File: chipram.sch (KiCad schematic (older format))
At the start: 28 parts, among them J500 Jumper_2_Bridged, U500 62402, U501 XX4256-15, U502 XX4256-15, U503 XX4256-15, U504 XX4256-15, U505 XX4256-15, U506 XX4256-15, U507 XX4256-15, U508 XX4256-15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

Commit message: Update footprints
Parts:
- C500, C501, C502, C503, C504, C505, C506, C507, C508, C540, C541: footprint (none) -> Capacitor_THT:C_Rect_L11.0mm_W2.8mm_P10.00mm_MKT
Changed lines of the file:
@@
 F 0 "C500" V 2848 10700 50  0000 C CNN
 F 1 "0.22uF" V 2939 10700 50  0000 C CNN
-F 2 "" H 3138 10550 50  0001 C CNN
+F 2 "Capacitor_THT:C_Rect_L11.0mm_W2.8mm_P10.00mm_MKT" H 3138 10550 50  0001 C CNN
 F 3 "~" H 3100 10700 50  0001 C CNN
 	1    3100 10700
@@
 F 0 "C501" V 7548 4300 50  0000 C CNN
 F 1 "0.33uF" V 7639 4300 50  0000 C CNN
-F 2 "" H 7838 4150 50  0001 C CNN
+F 2 "Capacitor_THT:C_Rect_L11.0mm_W2.8mm_P10.00mm_MKT" H 7838 4150 50  0001 C CNN
 F 3 "~" H 7800 4300 50  0001 C CNN
 	1    7800 4300
@@
 F 0 "C502" V 10048 4300 50  0000 C CNN
 F 1 "0.33uF" V 10139 4300 50  0000 C CNN
-F 2 "" H 10338 4150 50  0001 C CNN
+F 2 "Capacitor_THT:C_Rect_L11.0mm_W2.8mm_P10.00mm_MKT" H 10338 4150 50  0001 C CNN
 F 3 "~" H 10300 4300 50  0001 C CNN
 	1    10300 4300
@@
 F 0 "C503" V 12548 4300 50  0000 C CNN
 F 1 "0.33uF" V 12639 4300 50  0000 C CNN
-F 2 "" H 12838 4150 50  0001 C CNN
+F 2 "Capacitor_THT:C_Rect_L11.0mm_W2.8mm_P10.00mm_MKT" H 12838 4150 50  0001 C CNN
 F 3 "~" H 12800 4300 50  0001 C CNN
 	1    12800 4300
@@
 F 0 "C504" V 14548 4300 50  0000 C CNN
 F 1 "0.33uF" V 14639 4300 50  0000 C CNN
-F 2 "" H 14838 4150 50  0001 C CNN
+F 2 "Capacitor_THT:C_Rect_L11.0mm_W2.8mm_P10.00mm_MKT" H 14838 4150 50  0001 C CNN
 F 3 "~" H 14800 4300 50  0001 C CNN
 	1    14800 4300
@@
 F 0 "C508" V 14548 7300 50  0000 C CNN
 F 1 "0.33uF" V 14639 7300 50  0000 C CNN
-F 2 "" H 14838 7150 50  0001 C CNN
+F 2 "Capacitor_THT:C_Rect_L11.0mm_W2.8mm_P10.00mm_MKT" H 14838 7150 50  0001 C CNN
 F 3 "~" H 14800 7300 50  0001 C CNN
 	1    14800 7300
@@
 F 0 "C507" V 12498 7300 50  0000 C CNN
 F 1 "0.33uF" V 12589 7300 50  0000 C CNN
-F 2 "" H 12788 7150 50  0001 C CNN
+F 2 "Capacitor_THT:C_Rect_L11.0mm_W2.8mm_P10.00mm_MKT" H 12788 7150 50  0001 C CNN
 F 3 "~" H 12750 7300 50  0001 C CNN
 	1    12750 7300
@@
 F 0 "C506" V 10048 7300 50  0000 C CNN
 F 1 "0.33uF" V 10139 7300 50  0000 C CNN
-F 2 "" H 10338 7150 50  0001 C CNN
+F 2 "Capacitor_THT:C_Rect_L11.0mm_W2.8mm_P10.00mm_MKT" H 10338 7150 50  0001 C CNN
 F 3 "~" H 10300 7300 50  0001 C CNN
 	1    10300 7300
@@
 F 0 "C505" V 7548 7300 50  0000 C CNN
 F 1 "0.33uF" V 7639 7300 50  0000 C CNN
-F 2 "" H 7838 7150 50  0001 C CNN
+F 2 "Capacitor_THT:C_Rect_L11.0mm_W2.8mm_P10.00mm_MKT" H 7838 7150 50  0001 C CNN
 F 3 "~" H 7800 7300 50  0001 C CNN
 	1    7800 7300
@@
 F 0 "C540" H 2565 896 50  0000 L CNN
 F 1 "0.1uF" H 2565 805 50  0000 L CNN
-F 2 "" H 2488 700 50  0001 C CNN
+F 2 "Capacitor_THT:C_Rect_L11.0mm_W2.8mm_P10.00mm_MKT" H 2488 700 50  0001 C CNN
 F 3 "~" H 2450 850 50  0001 C CNN
 	1    2450 850
@@
 F 0 "C541" H 2615 2846 50  0000 L CNN
 F 1 "0.1uF" H 2615 2755 50  0000 L CNN
-F 2 "" H 2538 2650 50  0001 C CNN
+F 2 "Capacitor_THT:C_Rect_L11.0mm_W2.8mm_P10.00mm_MKT" H 2538 2650 50  0001 C CNN
 F 3 "~" H 2500 2800 50  0001 C CNN
 	1    2500 2800

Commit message: More placement
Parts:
- J500: footprint Connector_PinSocket_2.54mm:PinSocket_2x01_P2.54mm_Vertical -> Connector_PinHeader_2.54mm:PinHeader_2x01_P2.54mm_Vertical
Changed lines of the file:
@@
 F 0 "J500" H 1750 7603 50  0000 C CNN
 F 1 "Jumper_2_Bridged" H 1750 7604 50  0001 C CNN
-F 2 "Connector_PinSocket_2.54mm:PinSocket_2x01_P2.54mm_Vertical" H 1750 7500 50  0001 C CNN
+F 2 "Connector_PinHeader_2.54mm:PinHeader_2x01_P2.54mm_Vertical" H 1750 7500 50  0001 C CNN
 F 3 "~" H 1750 7500 50  0001 C CNN
 	1    1750 7500

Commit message: Make caps footprint smaller
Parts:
- C500, C501, C502, C503, C504, C505, C506, C507, C508, C540, C541: footprint Capacitor_THT:C_Rect_L11.0mm_W2.8mm_P10.00mm_MKT -> Capacitor_THT:C_Rect_L11.5mm_W2.0mm_P10.00mm_MKT
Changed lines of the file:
@@
 F 0 "C500" V 2848 10700 50  0000 C CNN
 F 1 "0.22uF" V 2939 10700 50  0000 C CNN
-F 2 "Capacitor_THT:C_Rect_L11.0mm_W2.8mm_P10.00mm_MKT" H 3138 10550 50  0001 C CNN
+F 2 "Capacitor_THT:C_Rect_L11.5mm_W2.0mm_P10.00mm_MKT" H 3138 10550 50  0001 C CNN
 F 3 "~" H 3100 10700 50  0001 C CNN
 	1    3100 10700
@@
 F 0 "C501" V 7548 4300 50  0000 C CNN
 F 1 "0.33uF" V 7639 4300 50  0000 C CNN
-F 2 "Capacitor_THT:C_Rect_L11.0mm_W2.8mm_P10.00mm_MKT" H 7838 4150 50  0001 C CNN
+F 2 "Capacitor_THT:C_Rect_L11.5mm_W2.0mm_P10.00mm_MKT" H 7838 4150 50  0001 C CNN
 F 3 "~" H 7800 4300 50  0001 C CNN
 	1    7800 4300
@@
 F 0 "C502" V 10048 4300 50  0000 C CNN
 F 1 "0.33uF" V 10139 4300 50  0000 C CNN
-F 2 "Capacitor_THT:C_Rect_L11.0mm_W2.8mm_P10.00mm_MKT" H 10338 4150 50  0001 C CNN
+F 2 "Capacitor_THT:C_Rect_L11.5mm_W2.0mm_P10.00mm_MKT" H 10338 4150 50  0001 C CNN
 F 3 "~" H 10300 4300 50  0001 C CNN
 	1    10300 4300
@@
 F 0 "C503" V 12548 4300 50  0000 C CNN
 F 1 "0.33uF" V 12639 4300 50  0000 C CNN
-F 2 "Capacitor_THT:C_Rect_L11.0mm_W2.8mm_P10.00mm_MKT" H 12838 4150 50  0001 C CNN
+F 2 "Capacitor_THT:C_Rect_L11.5mm_W2.0mm_P10.00mm_MKT" H 12838 4150 50  0001 C CNN
 F 3 "~" H 12800 4300 50  0001 C CNN
 	1    12800 4300
@@
 F 0 "C504" V 14548 4300 50  0000 C CNN
 F 1 "0.33uF" V 14639 4300 50  0000 C CNN
-F 2 "Capacitor_THT:C_Rect_L11.0mm_W2.8mm_P10.00mm_MKT" H 14838 4150 50  0001 C CNN
+F 2 "Capacitor_THT:C_Rect_L11.5mm_W2.0mm_P10.00mm_MKT" H 14838 4150 50  0001 C CNN
 F 3 "~" H 14800 4300 50  0001 C CNN
 	1    14800 4300
@@
 F 0 "C508" V 14548 7300 50  0000 C CNN
 F 1 "0.33uF" V 14639 7300 50  0000 C CNN
-F 2 "Capacitor_THT:C_Rect_L11.0mm_W2.8mm_P10.00mm_MKT" H 14838 7150 50  0001 C CNN
+F 2 "Capacitor_THT:C_Rect_L11.5mm_W2.0mm_P10.00mm_MKT" H 14838 7150 50  0001 C CNN
 F 3 "~" H 14800 7300 50  0001 C CNN
 	1    14800 7300
@@
 F 0 "C507" V 12498 7300 50  0000 C CNN
 F 1 "0.33uF" V 12589 7300 50  0000 C CNN
-F 2 "Capacitor_THT:C_Rect_L11.0mm_W2.8mm_P10.00mm_MKT" H 12788 7150 50  0001 C CNN
+F 2 "Capacitor_THT:C_Rect_L11.5mm_W2.0mm_P10.00mm_MKT" H 12788 7150 50  0001 C CNN
 F 3 "~" H 12750 7300 50  0001 C CNN
 	1    12750 7300
@@
 F 0 "C506" V 10048 7300 50  0000 C CNN
 F 1 "0.33uF" V 10139 7300 50  0000 C CNN
-F 2 "Capacitor_THT:C_Rect_L11.0mm_W2.8mm_P10.00mm_MKT" H 10338 7150 50  0001 C CNN
+F 2 "Capacitor_THT:C_Rect_L11.5mm_W2.0mm_P10.00mm_MKT" H 10338 7150 50  0001 C CNN
 F 3 "~" H 10300 7300 50  0001 C CNN
 	1    10300 7300
@@
 F 0 "C505" V 7548 7300 50  0000 C CNN
 F 1 "0.33uF" V 7639 7300 50  0000 C CNN
-F 2 "Capacitor_THT:C_Rect_L11.0mm_W2.8mm_P10.00mm_MKT" H 7838 7150 50  0001 C CNN
+F 2 "Capacitor_THT:C_Rect_L11.5mm_W2.0mm_P10.00mm_MKT" H 7838 7150 50  0001 C CNN
 F 3 "~" H 7800 7300 50  0001 C CNN
 	1    7800 7300
@@
 F 0 "C540" H 2565 896 50  0000 L CNN
 F 1 "0.1uF" H 2565 805 50  0000 L CNN
-F 2 "Capacitor_THT:C_Rect_L11.0mm_W2.8mm_P10.00mm_MKT" H 2488 700 50  0001 C CNN
+F 2 "Capacitor_THT:C_Rect_L11.5mm_W2.0mm_P10.00mm_MKT" H 2488 700 50  0001 C CNN
 F 3 "~" H 2450 850 50  0001 C CNN
 	1    2450 850
@@
 F 0 "C541" H 2615 2846 50  0000 L CNN
 F 1 "0.1uF" H 2615 2755 50  0000 L CNN
-F 2 "Capacitor_THT:C_Rect_L11.0mm_W2.8mm_P10.00mm_MKT" H 2538 2650 50  0001 C CNN
+F 2 "Capacitor_THT:C_Rect_L11.5mm_W2.0mm_P10.00mm_MKT" H 2538 2650 50  0001 C CNN
 F 3 "~" H 2500 2800 50  0001 C CNN
 	1    2500 2800

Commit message: Switch footprints for suitable modern replacements
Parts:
- C500, C501, C502, C503, C504, C505, C506, C507, C508: footprint Capacitor_THT:C_Rect_L11.5mm_W2.0mm_P10.00mm_MKT -> Capacitor_THT:C_Rect_L11.5mm_W4.0mm_P10.00mm_MKT
- C540, C541: footprint Capacitor_THT:C_Rect_L11.5mm_W2.0mm_P10.00mm_MKT -> Capacitor_THT:C_Rect_L11.5mm_W2.6mm_P10.00mm_MKT
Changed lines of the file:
@@
 F 0 "C500" V 2848 10700 50  0000 C CNN
 F 1 "0.22uF" V 2939 10700 50  0000 C CNN
-F 2 "Capacitor_THT:C_Rect_L11.5mm_W2.0mm_P10.00mm_MKT" H 3138 10550 50  0001 C CNN
+F 2 "Capacitor_THT:C_Rect_L11.5mm_W4.0mm_P10.00mm_MKT" H 3138 10550 50  0001 C CNN
 F 3 "~" H 3100 10700 50  0001 C CNN
 	1    3100 10700
@@
 F 0 "C501" V 7548 4300 50  0000 C CNN
 F 1 "0.33uF" V 7639 4300 50  0000 C CNN
-F 2 "Capacitor_THT:C_Rect_L11.5mm_W2.0mm_P10.00mm_MKT" H 7838 4150 50  0001 C CNN
+F 2 "Capacitor_THT:C_Rect_L11.5mm_W4.0mm_P10.00mm_MKT" H 7838 4150 50  0001 C CNN
 F 3 "~" H 7800 4300 50  0001 C CNN
 	1    7800 4300
@@
 F 0 "C502" V 10048 4300 50  0000 C CNN
 F 1 "0.33uF" V 10139 4300 50  0000 C CNN
-F 2 "Capacitor_THT:C_Rect_L11.5mm_W2.0mm_P10.00mm_MKT" H 10338 4150 50  0001 C CNN
+F 2 "Capacitor_THT:C_Rect_L11.5mm_W4.0mm_P10.00mm_MKT" H 10338 4150 50  0001 C CNN
 F 3 "~" H 10300 4300 50  0001 C CNN
 	1    10300 4300
@@
 F 0 "C503" V 12548 4300 50  0000 C CNN
 F 1 "0.33uF" V 12639 4300 50  0000 C CNN
-F 2 "Capacitor_THT:C_Rect_L11.5mm_W2.0mm_P10.00mm_MKT" H 12838 4150 50  0001 C CNN
+F 2 "Capacitor_THT:C_Rect_L11.5mm_W4.0mm_P10.00mm_MKT" H 12838 4150 50  0001 C CNN
 F 3 "~" H 12800 4300 50  0001 C CNN
 	1    12800 4300
@@
 F 0 "C504" V 14548 4300 50  0000 C CNN
 F 1 "0.33uF" V 14639 4300 50  0000 C CNN
-F 2 "Capacitor_THT:C_Rect_L11.5mm_W2.0mm_P10.00mm_MKT" H 14838 4150 50  0001 C CNN
+F 2 "Capacitor_THT:C_Rect_L11.5mm_W4.0mm_P10.00mm_MKT" H 14838 4150 50  0001 C CNN
 F 3 "~" H 14800 4300 50  0001 C CNN
 	1    14800 4300
@@
 F 0 "C508" V 14548 7300 50  0000 C CNN
 F 1 "0.33uF" V 14639 7300 50  0000 C CNN
-F 2 "Capacitor_THT:C_Rect_L11.5mm_W2.0mm_P10.00mm_MKT" H 14838 7150 50  0001 C CNN
+F 2 "Capacitor_THT:C_Rect_L11.5mm_W4.0mm_P10.00mm_MKT" H 14838 7150 50  0001 C CNN
 F 3 "~" H 14800 7300 50  0001 C CNN
 	1    14800 7300
@@
 F 0 "C507" V 12498 7300 50  0000 C CNN
 F 1 "0.33uF" V 12589 7300 50  0000 C CNN
-F 2 "Capacitor_THT:C_Rect_L11.5mm_W2.0mm_P10.00mm_MKT" H 12788 7150 50  0001 C CNN
+F 2 "Capacitor_THT:C_Rect_L11.5mm_W4.0mm_P10.00mm_MKT" H 12788 7150 50  0001 C CNN
 F 3 "~" H 12750 7300 50  0001 C CNN
 	1    12750 7300
@@
 F 0 "C506" V 10048 7300 50  0000 C CNN
 F 1 "0.33uF" V 10139 7300 50  0000 C CNN
-F 2 "Capacitor_THT:C_Rect_L11.5mm_W2.0mm_P10.00mm_MKT" H 10338 7150 50  0001 C CNN
+F 2 "Capacitor_THT:C_Rect_L11.5mm_W4.0mm_P10.00mm_MKT" H 10338 7150 50  0001 C CNN
 F 3 "~" H 10300 7300 50  0001 C CNN
 	1    10300 7300
@@
 F 0 "C505" V 7548 7300 50  0000 C CNN
 F 1 "0.33uF" V 7639 7300 50  0000 C CNN
-F 2 "Capacitor_THT:C_Rect_L11.5mm_W2.0mm_P10.00mm_MKT" H 7838 7150 50  0001 C CNN
+F 2 "Capacitor_THT:C_Rect_L11.5mm_W4.0mm_P10.00mm_MKT" H 7838 7150 50  0001 C CNN
 F 3 "~" H 7800 7300 50  0001 C CNN
 	1    7800 7300
@@
 F 0 "C540" H 2565 896 50  0000 L CNN
 F 1 "0.1uF" H 2565 805 50  0000 L CNN
-F 2 "Capacitor_THT:C_Rect_L11.5mm_W2.0mm_P10.00mm_MKT" H 2488 700 50  0001 C CNN
+F 2 "Capacitor_THT:C_Rect_L11.5mm_W2.6mm_P10.00mm_MKT" H 2488 700 50  0001 C CNN
 F 3 "~" H 2450 850 50  0001 C CNN
 	1    2450 850
@@
 F 0 "C541" H 2615 2846 50  0000 L CNN
 F 1 "0.1uF" H 2615 2755 50  0000 L CNN
-F 2 "Capacitor_THT:C_Rect_L11.5mm_W2.0mm_P10.00mm_MKT" H 2538 2650 50  0001 C CNN
+F 2 "Capacitor_THT:C_Rect_L11.5mm_W2.6mm_P10.00mm_MKT" H 2538 2650 50  0001 C CNN
 F 3 "~" H 2500 2800 50  0001 C CNN
 	1    2500 2800

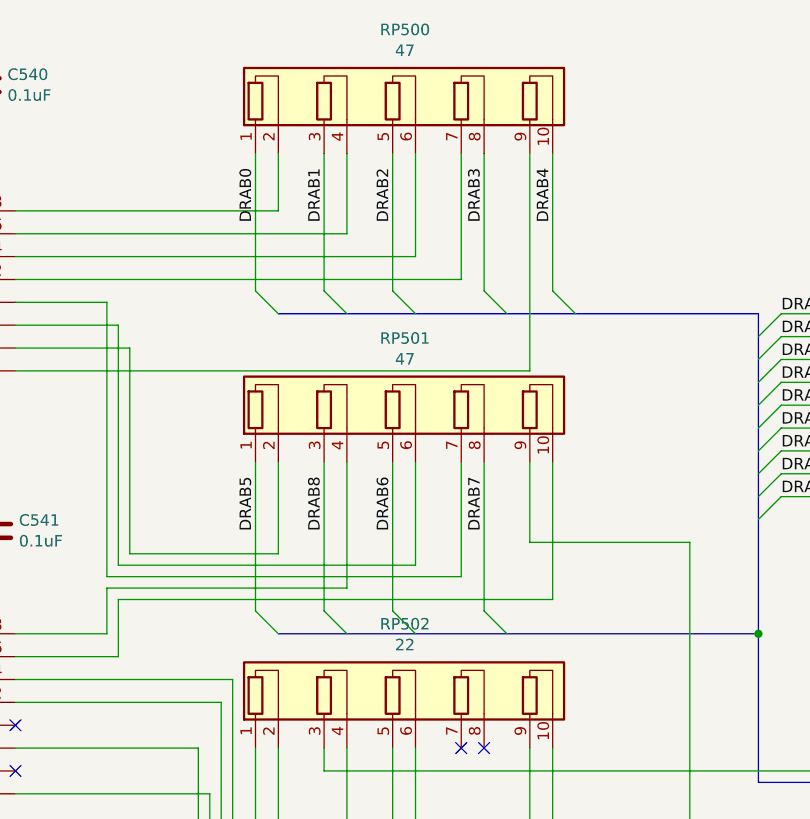
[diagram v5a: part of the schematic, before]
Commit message: Some footprints updates; Add all Mouser references
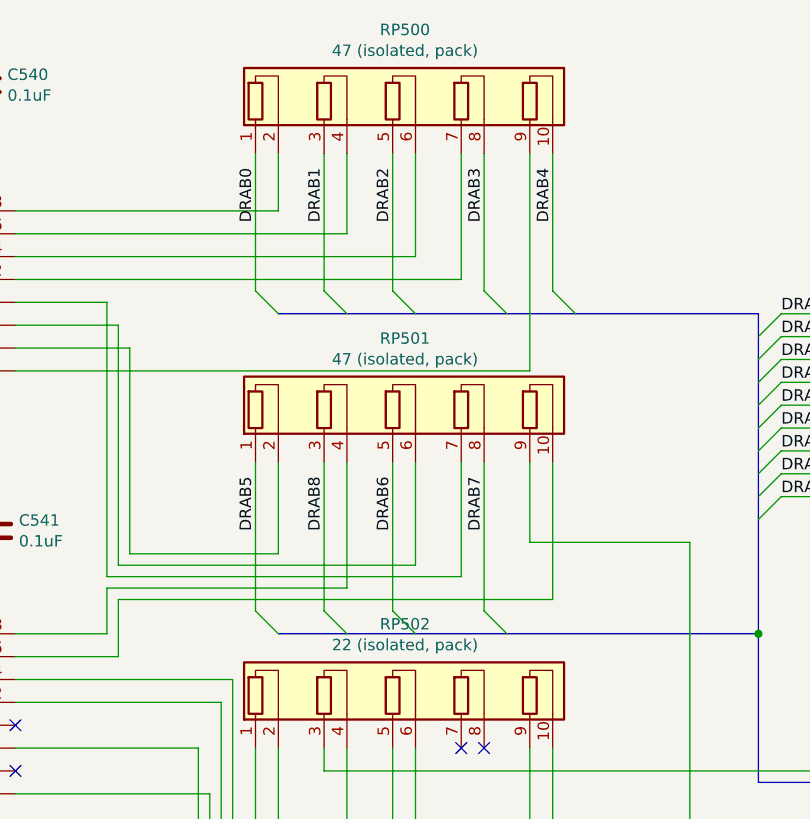
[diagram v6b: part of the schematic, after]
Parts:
- C500: RefOrder (none) -> 594-A224K20X7RF5TAA
- C501, C502, C503, C504, C505, C506, C507, C508: RefOrder (none) -> 581-SA305C334KAA
- C540, C541: RefOrder (none) -> 581-SA105C104KARC
- R500: RefOrder (none) -> 603-CFR-25JT-52-4K7
- RP500, RP501: value 47 -> 47 (isolated, pack); RefOrder (none) -> 652-4610X-2LF-47
- RP502: value 22 -> 22 (isolated, pack); RefOrder (none) -> 652-4610X-2LF-22
- RP503: RefOrder (none) -> 652-4610X-1LF-470
- U540, U541: RefOrder (none) -> 595-SN74F244N
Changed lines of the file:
@@
 F 2 "Package_DIP:DIP-20_W7.62mm_Socket" H 2100 1900 50  0001 C CNN
 F 3 "http://www.ti.com/lit/gpn/sn74F244" H 2100 1900 50  0001 C CNN
+F 4 "595-SN74F244N" H 2100 1900 50  0001 C CNN "RefOrder"
 	1    2100 1900
 	1    0    0    -1
@@
 F 2 "Package_DIP:DIP-20_W7.62mm_Socket" H 2100 3750 50  0001 C CNN
 F 3 "http://www.ti.com/lit/gpn/sn74F244" H 2100 3750 50  0001 C CNN
+F 4 "595-SN74F244N" H 2100 3750 50  0001 C CNN "RefOrder"
 	1    2100 3750
 	1    0    0    -1
@@
 F 2 "Capacitor_THT:C_Rect_L11.5mm_W4.0mm_P10.00mm_MKT" H 3138 10550 50  0001 C CNN
 F 3 "~" H 3100 10700 50  0001 C CNN
+F 4 "594-A224K20X7RF5TAA" H 3100 10700 50  0001 C CNN "RefOrder"
 	1    3100 10700
 	0    1    1    0
@@
 F 2 "Resistor_THT:R_Axial_DIN0207_L6.3mm_D2.5mm_P10.16mm_Horizontal" V 1230 7250 50  0001 C CNN
 F 3 "~" H 1300 7250 50  0001 C CNN
+F 4 "603-CFR-25JT-52-4K7" H 1300 7250 50  0001 C CNN "RefOrder"
 	1    1300 7250
 	1    0    0    -1
@@
 F 2 "Capacitor_THT:C_Rect_L11.5mm_W4.0mm_P10.00mm_MKT" H 7838 4150 50  0001 C CNN
 F 3 "~" H 7800 4300 50  0001 C CNN
+F 4 "581-SA305C334KAA" H 7800 4300 50  0001 C CNN "RefOrder"
 	1    7800 4300
 	0    1    1    0
@@
 F 2 "Capacitor_THT:C_Rect_L11.5mm_W4.0mm_P10.00mm_MKT" H 10338 4150 50  0001 C CNN
 F 3 "~" H 10300 4300 50  0001 C CNN
+F 4 "581-SA305C334KAA" H 10300 4300 50  0001 C CNN "RefOrder"
 	1    10300 4300
 	0    1    1    0
@@
 F 2 "Capacitor_THT:C_Rect_L11.5mm_W4.0mm_P10.00mm_MKT" H 12838 4150 50  0001 C CNN
 F 3 "~" H 12800 4300 50  0001 C CNN
+F 4 "581-SA305C334KAA" H 12800 4300 50  0001 C CNN "RefOrder"
 	1    12800 4300
 	0    1    1    0
@@
 F 2 "Capacitor_THT:C_Rect_L11.5mm_W4.0mm_P10.00mm_MKT" H 14838 4150 50  0001 C CNN
 F 3 "~" H 14800 4300 50  0001 C CNN
+F 4 "581-SA305C334KAA" H 14800 4300 50  0001 C CNN "RefOrder"
 	1    14800 4300
 	0    1    1    0
@@
 F 2 "Capacitor_THT:C_Rect_L11.5mm_W4.0mm_P10.00mm_MKT" H 14838 7150 50  0001 C CNN
 F 3 "~" H 14800 7300 50  0001 C CNN
+F 4 "581-SA305C334KAA" H 14800 7300 50  0001 C CNN "RefOrder"
 	1    14800 7300
 	0    1    1    0
@@
 F 2 "Capacitor_THT:C_Rect_L11.5mm_W4.0mm_P10.00mm_MKT" H 12788 7150 50  0001 C CNN
 F 3 "~" H 12750 7300 50  0001 C CNN
+F 4 "581-SA305C334KAA" H 12750 7300 50  0001 C CNN "RefOrder"
 	1    12750 7300
 	0    1    1    0
@@
 F 2 "Capacitor_THT:C_Rect_L11.5mm_W4.0mm_P10.00mm_MKT" H 10338 7150 50  0001 C CNN
 F 3 "~" H 10300 7300 50  0001 C CNN
+F 4 "581-SA305C334KAA" H 10300 7300 50  0001 C CNN "RefOrder"
 	1    10300 7300
 	0    1    1    0
@@
 F 2 "Capacitor_THT:C_Rect_L11.5mm_W4.0mm_P10.00mm_MKT" H 7838 7150 50  0001 C CNN
 F 3 "~" H 7800 7300 50  0001 C CNN
+F 4 "581-SA305C334KAA" H 7800 7300 50  0001 C CNN "RefOrder"
 	1    7800 7300
 	0    1    1    0
@@
 F 2 "Resistor_THT:R_Array_SIP10" V 7125 2250 50  0001 C CNN
 F 3 "http://www.vishay.com/docs/31509/csc.pdf" H 6550 2250 50  0001 C CNN
+F 4 "652-4610X-1LF-470" H 6550 2250 50  0001 C CNN "RefOrder"
 	1    6550 2250
 	0    1    1    0
@@
 P 4250 950
 F 0 "RP500" H 4304 1292 50  0000 C CNN
-F 1 "47" H 4304 1201 50  0000 C CNN
+F 1 "47 (isolated, pack)" H 4304 1201 50  0000 C CNN
 F 2 "Resistor_THT:R_Array_SIP10" V 5125 950 50  0001 C CNN
 F 3 "http://www.vishay.com/docs/31509/csc.pdf" H 4250 950 50  0001 C CNN
+F 4 "652-4610X-2LF-47" H 4250 950 50  0001 C CNN "RefOrder"
 	1    4250 950
 	1    0    0    -1
@@
 P 4250 2300
 F 0 "RP501" H 4304 2642 50  0000 C CNN
-F 1 "47" H 4304 2551 50  0000 C CNN
+F 1 "47 (isolated, pack)" H 4304 2551 50  0000 C CNN
 F 2 "Resistor_THT:R_Array_SIP10" V 5125 2300 50  0001 C CNN
 F 3 "http://www.vishay.com/docs/31509/csc.pdf" H 4250 2300 50  0001 C CNN
+F 4 "652-4610X-2LF-47" H 4250 2300 50  0001 C CNN "RefOrder"
 	1    4250 2300
 	1    0    0    -1
@@
 P 4250 3550
 F 0 "RP502" H 4304 3892 50  0000 C CNN
-F 1 "22" H 4304 3801 50  0000 C CNN
+F 1 "22 (isolated, pack)" H 4304 3801 50  0000 C CNN
 F 2 "Resistor_THT:R_Array_SIP10" V 5125 3550 50  0001 C CNN
 F 3 "http://www.vishay.com/docs/31509/csc.pdf" H 4250 3550 50  0001 C CNN
+F 4 "652-4610X-2LF-22" H 4250 3550 50  0001 C CNN "RefOrder"
 	1    4250 3550
 	1    0    0    -1
@@
 F 2 "Capacitor_THT:C_Rect_L11.5mm_W2.6mm_P10.00mm_MKT" H 2488 700 50  0001 C CNN
 F 3 "~" H 2450 850 50  0001 C CNN
+F 4 "581-SA105C104KARC" H 2450 850 50  0001 C CNN "RefOrder"
 	1    2450 850
 	1    0    0    -1
@@
 F 2 "Capacitor_THT:C_Rect_L11.5mm_W2.6mm_P10.00mm_MKT" H 2538 2650 50  0001 C CNN
 F 3 "~" H 2500 2800 50  0001 C CNN
+F 4 "581-SA105C104KARC" H 2500 2800 50  0001 C CNN "RefOrder"
 	1    2500 2800
 	1    0    0    -1

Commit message: Got the components, reduce some footprints
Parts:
- C500: footprint Capacitor_THT:C_Rect_L11.5mm_W4.0mm_P10.00mm_MKT -> Capacitor_THT:C_Rect_L11.5mm_W2.6mm_P10.00mm_MKT
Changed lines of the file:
@@
 F 0 "C500" V 2848 10700 50  0000 C CNN
 F 1 "0.22uF" V 2939 10700 50  0000 C CNN
-F 2 "Capacitor_THT:C_Rect_L11.5mm_W4.0mm_P10.00mm_MKT" H 3138 10550 50  0001 C CNN
+F 2 "Capacitor_THT:C_Rect_L11.5mm_W2.6mm_P10.00mm_MKT" H 3138 10550 50  0001 C CNN
 F 3 "~" H 3100 10700 50  0001 C CNN
 F 4 "594-A224K20X7RF5TAA" H 3100 10700 50  0001 C CNN "RefOrder"
